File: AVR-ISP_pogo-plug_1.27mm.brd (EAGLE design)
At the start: 12.4 x 30.5 mm, 1 part

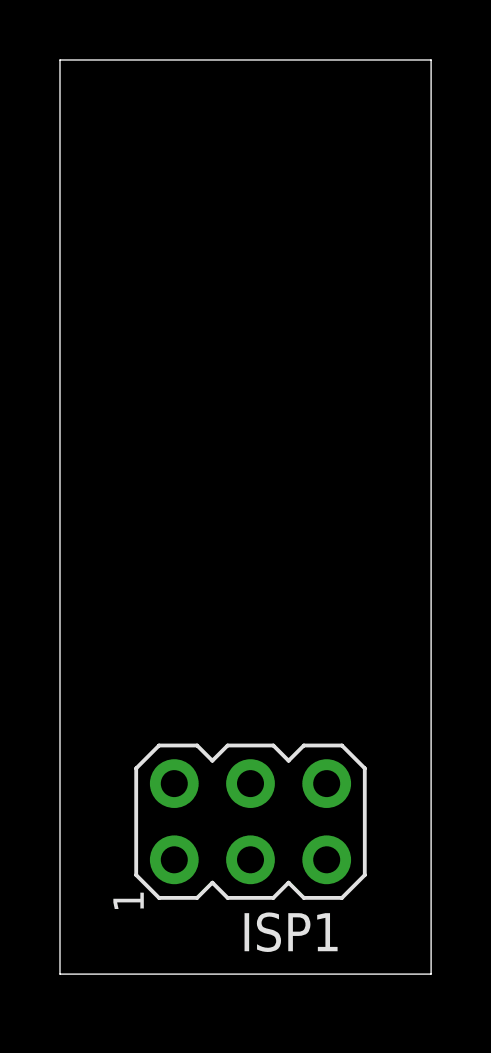
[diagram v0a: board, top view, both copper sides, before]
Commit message: done, fliped pins from source.
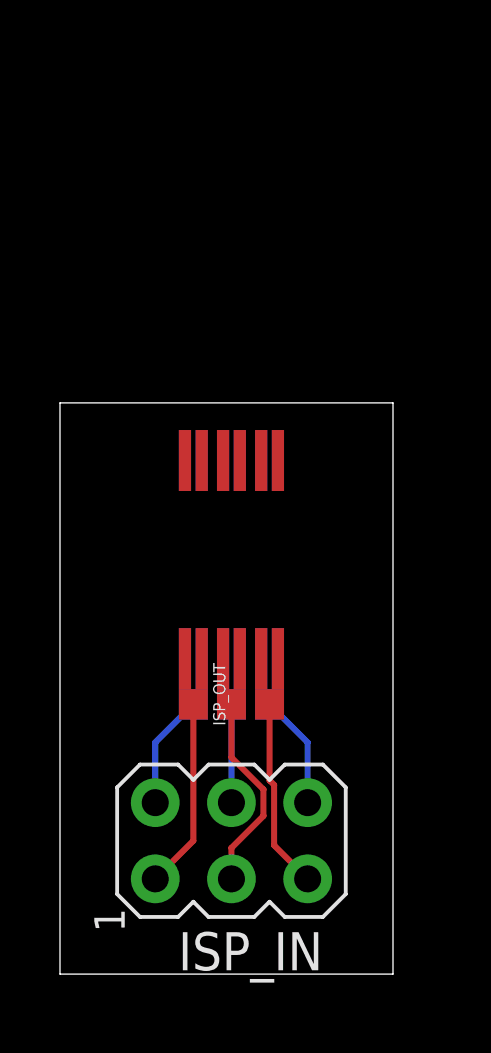
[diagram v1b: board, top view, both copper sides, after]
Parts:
- removed ISP1: AVRISP-6, TinyTony_ShenzenReady:AVRISP
- added ISP_IN: AVRISP-6, TinyTony_ShenzenReady:AVRISP
- added ISP_OUT: AVRISPPOGOPINS, TinyTony_ShenzenReady:POGO-50MIL-6PADS
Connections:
- removed net GND: ISP1.6
- removed net VCC: ISP1.2
- new net N$1: ISP_IN.2, ISP_OUT.2
- new net N$2: ISP_IN.4, ISP_OUT.4
- new net N$3: ISP_IN.6, ISP_OUT.6
- new net N$4: ISP_IN.1, ISP_OUT.1
- new net N$5: ISP_IN.3, ISP_OUT.3
- new net N$6: ISP_IN.5, ISP_OUT.5
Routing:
- net N$5: track 0.00 -> 6.70 mm
- net N$4: track 0.00 -> 6.34 mm
- net N$6: track 0.00 -> 6.34 mm
- net N$3: track 0.00 -> 3.80 mm
- net N$1: track 0.00 -> 3.80 mm
- net N$2: track 0.00 -> 3.28 mm
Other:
- board size 12.4 x 30.5 mm -> 11.1 x 19 mm
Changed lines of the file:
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@@
 <setting verticaltext="up"/>
 </settings>
-<grid distance="50" unitdist="mil" unit="mil" style="lines" multiple="1" display="no" altdistance="5" altunitdist="mil" altunit="mil"/>
+<grid distance="25" unitdist="mil" unit="mil" style="lines" multiple="1" display="yes" altdistance="1" altunitdist="mil" altunit="mil"/>
 <layers>
 <layer number="1" name="Top" color="4" fill="1" visible="yes" active="yes"/>
@@
 <board>
 <plain>
-<wire x1="0" y1="0" x2="12.37" y2="0" width="0" layer="20"/>
-<wire x1="12.37" y1="0" x2="12.37" y2="30.47" width="0" layer="20"/>
-<wire x1="12.37" y1="30.47" x2="0" y2="30.47" width="0" layer="20"/>
-<wire x1="0" y1="30.47" x2="0" y2="0" width="0" layer="20"/>
+<wire x1="0" y1="0" x2="11.1" y2="0" width="0" layer="20"/>
+<wire x1="11.1" y1="0" x2="11.1" y2="19.04" width="0" layer="20"/>
+<wire x1="11.1" y1="19.04" x2="0" y2="19.04" width="0" layer="20"/>
+<wire x1="0" y1="19.04" x2="0" y2="0" width="0" layer="20"/>
 </plain>
 <attributes>
@@
 </autorouter>
 <elements>
-<element name="ISP1" library="TinyTony_ShenzenReady" package="AVRISP" value="AVRISP-6" x="6.35" y="5.08" rot="R90"/>
+<element name="ISP_IN" library="TinyTony_ShenzenReady" package="AVRISP" value="AVRISP-6" x="5.715" y="4.445" rot="R90">
+<attribute name="SPICEPREFIX" value="X" x="5.715" y="4.445" size="1.778" layer="27" rot="R90" display="off"/>
+</element>
+<element name="ISP_OUT" library="TinyTony_ShenzenReady" package="POGO-50MIL-6PADS" value="AVRISPPOGOPINS" x="5.715" y="8.4836"/>
 </elements>
 <signals>
-<signal name="GND">
-<contactref element="ISP1" pad="6"/>
-</signal>
-<signal name="VCC">
-<contactref element="ISP1" pad="2"/>
+<signal name="N$1">
+<contactref element="ISP_IN" pad="2"/>
+<contactref element="ISP_OUT" pad="2"/>
+<wire x1="3.175" y1="5.715" x2="3.175" y2="7.7216" width="0.2032" layer="16"/>
+<wire x1="3.175" y1="7.7216" x2="4.445" y2="8.9916" width="0.2032" layer="16"/>
+</signal>
+<signal name="N$2">
+<contactref element="ISP_OUT" pad="4"/>
+<contactref element="ISP_IN" pad="4"/>
+<wire x1="5.715" y1="5.715" x2="5.715" y2="8.9916" width="0.2032" layer="16"/>
+</signal>
+<signal name="N$3">
+<contactref element="ISP_IN" pad="6"/>
+<contactref element="ISP_OUT" pad="6"/>
+<wire x1="8.255" y1="5.715" x2="8.255" y2="7.7216" width="0.2032" layer="16"/>
+<wire x1="8.255" y1="7.7216" x2="6.985" y2="8.9916" width="0.2032" layer="16"/>
+</signal>
+<signal name="N$4">
+<contactref element="ISP_OUT" pad="1"/>
+<contactref element="ISP_IN" pad="1"/>
+<wire x1="4.445" y1="8.9916" x2="4.445" y2="4.445" width="0.2032" layer="1"/>
+<wire x1="4.445" y1="4.445" x2="3.175" y2="3.175" width="0.2032" layer="1"/>
+</signal>
+<signal name="N$5">
+<contactref element="ISP_OUT" pad="3"/>
+<contactref element="ISP_IN" pad="3"/>
+<wire x1="6.7818" y1="5.2731125" x2="6.7818" y2="6.1568875" width="0.2032" layer="1"/>
+<wire x1="5.715" y1="3.175" x2="5.715" y2="4.2063125" width="0.2032" layer="1"/>
+<wire x1="5.715" y1="7.2236875" x2="5.715" y2="8.9916" width="0.2032" layer="1"/>
+<wire x1="5.715" y1="4.2063125" x2="6.7818" y2="5.2731125" width="0.2032" layer="1"/>
+<wire x1="6.7818" y1="6.1568875" x2="5.715" y2="7.2236875" width="0.2032" layer="1"/>
+</signal>
+<signal name="N$6">
+<contactref element="ISP_IN" pad="5"/>
+<contactref element="ISP_OUT" pad="5"/>
+<wire x1="6.985" y1="8.9916" x2="6.985" y2="6.4565875" width="0.2032" layer="1"/>
+<wire x1="6.985" y1="6.4565875" x2="7.1374" y2="6.3041875" width="0.2032" layer="1"/>
+<wire x1="7.1374" y1="4.2926" x2="8.255" y2="3.175" width="0.2032" layer="1"/>
+<wire x1="7.1374" y1="6.3041875" x2="7.1374" y2="4.2926" width="0.2032" layer="1"/>
 </signal>
 </signals>
